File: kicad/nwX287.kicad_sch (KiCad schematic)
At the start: 5 parts, among them U1 bq4285, U2 socket, Y1 32.768kHz 6pF

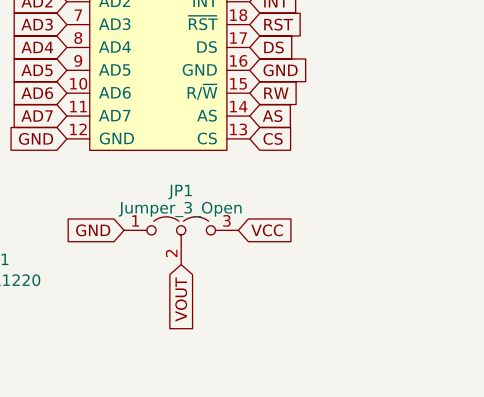
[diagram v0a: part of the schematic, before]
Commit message: CR2032 vertical holder and holes for easier oscillator mount
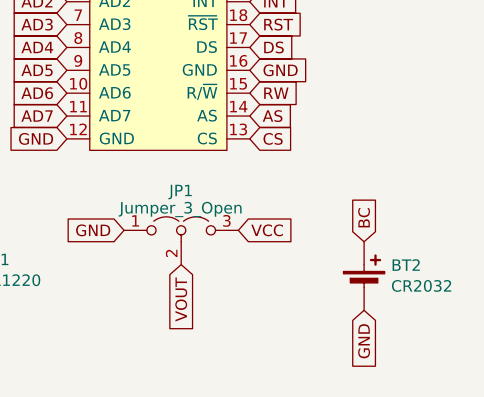
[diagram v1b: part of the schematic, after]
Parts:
- added BT2: CR2032, Rime:CR2032_Vertical, symbol Device:Battery_Cell
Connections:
- net BC: now also BT2.1 (+)
- net GND: now also BT2.2 (-)
